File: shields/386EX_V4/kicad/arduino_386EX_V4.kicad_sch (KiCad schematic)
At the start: 48 parts, among them J1 Conn_01x02_Pin, J2 JTAG, J3 Conn_01x04_Pin, J4 Conn_01x04_Pin, J5 Conn_01x04_Pin, J6 SERIAL0, J9 WP Jumper, U1 AT24CS01-STUM, U11 I386EX_PQFP, U2 ULN2003A, U3 SN74LV14A

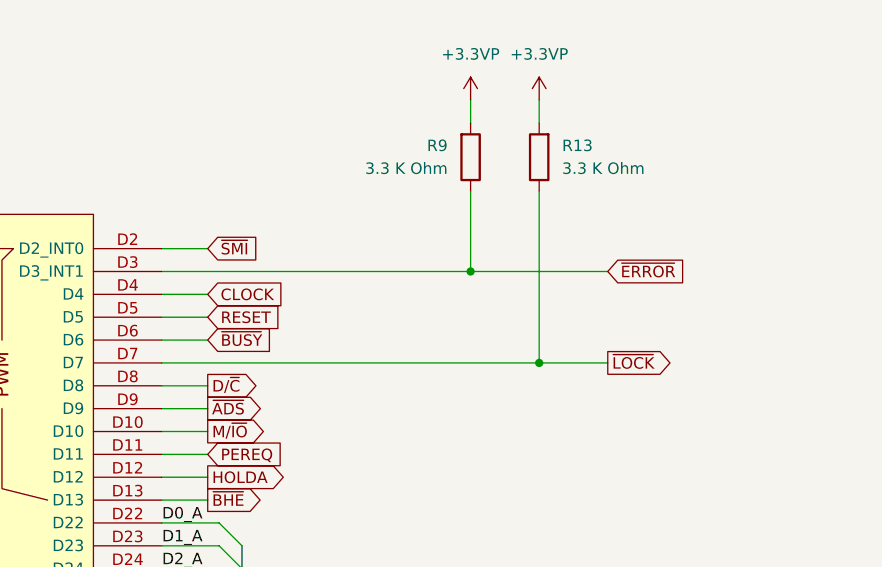
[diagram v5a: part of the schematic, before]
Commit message: Fixed bug from previous commit, R13 was wired to ~LOCK, was supposed to be to ~BUSY, corrected in this commit.
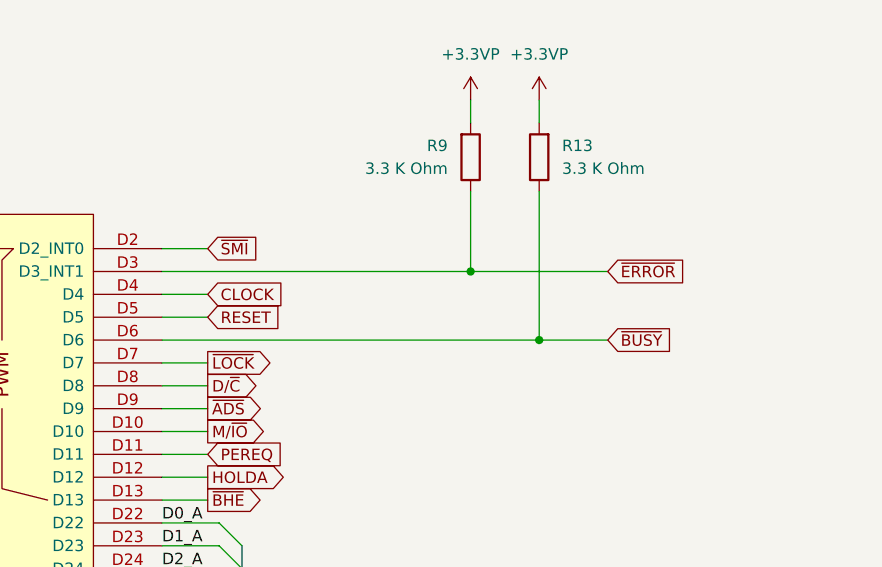
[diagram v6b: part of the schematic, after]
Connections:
- net ~{BUSY}: now also R13.1
- net ~{LOCK}: no longer R13.1
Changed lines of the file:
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@@
 	)
 	(junction
-		(at 208.28 60.96)
-		(diameter 0)
-		(color 0 0 0 0)
-	)
-	(junction
 		(at 63.5 241.3)
 		(diameter 0)
@@
 	)
 	(junction
+		(at 208.28 58.42)
+		(diameter 0)
+		(color 0 0 0 0)
+	)
+	(junction
 		(at 257.81 261.62)
 		(diameter 0)
@@
 	(wire
 		(pts
-			(xy 171.45 58.42) (xy 166.37 58.42)
+			(xy 215.9 58.42) (xy 208.28 58.42)
 		)
 		(stroke
@@
 	(wire
 		(pts
-			(xy 215.9 60.96) (xy 208.28 60.96)
+			(xy 166.37 60.96) (xy 171.45 60.96)
 		)
 		(stroke
@@
 	(wire
 		(pts
+			(xy 208.28 58.42) (xy 166.37 58.42)
+		)
+		(stroke
+			(width 0)
+			(type default)
+		)
+	)
+	(wire
+		(pts
 			(xy 429.26 34.29) (xy 429.26 36.83)
 		)
@@
 	(wire
 		(pts
+			(xy 208.28 41.91) (xy 208.28 58.42)
+		)
+		(stroke
+			(width 0)
+			(type default)
+		)
+	)
+	(wire
+		(pts
 			(xy 454.66 176.53) (xy 458.47 176.53)
 		)
@@
 	(wire
 		(pts
-			(xy 208.28 41.91) (xy 208.28 60.96)
-		)
-		(stroke
-			(width 0)
-			(type default)
-		)
-	)
-	(wire
-		(pts
 			(xy 50.8 323.85) (xy 50.8 332.74)
 		)
@@
 	(wire
 		(pts
-			(xy 208.28 60.96) (xy 166.37 60.96)
-		)
-		(stroke
-			(width 0)
-			(type default)
-		)
-	)
-	(wire
-		(pts
 			(xy 450.85 83.82) (xy 450.85 80.01)
 		)
@@
 	(global_label "~{BUSY}"
 		(shape input)
-		(at 171.45 58.42 0)
+		(at 215.9 58.42 0)
 		(fields_autoplaced yes)
 		(effects
@@
 		)
 		(property "Intersheetrefs" "${INTERSHEET_REFS}"
-			(at 179.3338 58.42 0)
+			(at 223.7838 58.42 0)
 			(effects
 				(font
@@
 	(global_label "~{LOCK}"
 		(shape output)
-		(at 215.9 60.96 0)
+		(at 171.45 60.96 0)
 		(fields_autoplaced yes)
 		(effects
@@
 		)
 		(property "Intersheetrefs" "${INTERSHEET_REFS}"
-			(at 223.7838 60.96 0)
+			(at 179.3338 60.96 0)
 			(effects
 				(font
